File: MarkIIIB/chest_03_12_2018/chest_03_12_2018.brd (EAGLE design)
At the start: 24.9 x 22.3 mm, 15 parts, among them P100 503148-0890, U101 BNO055

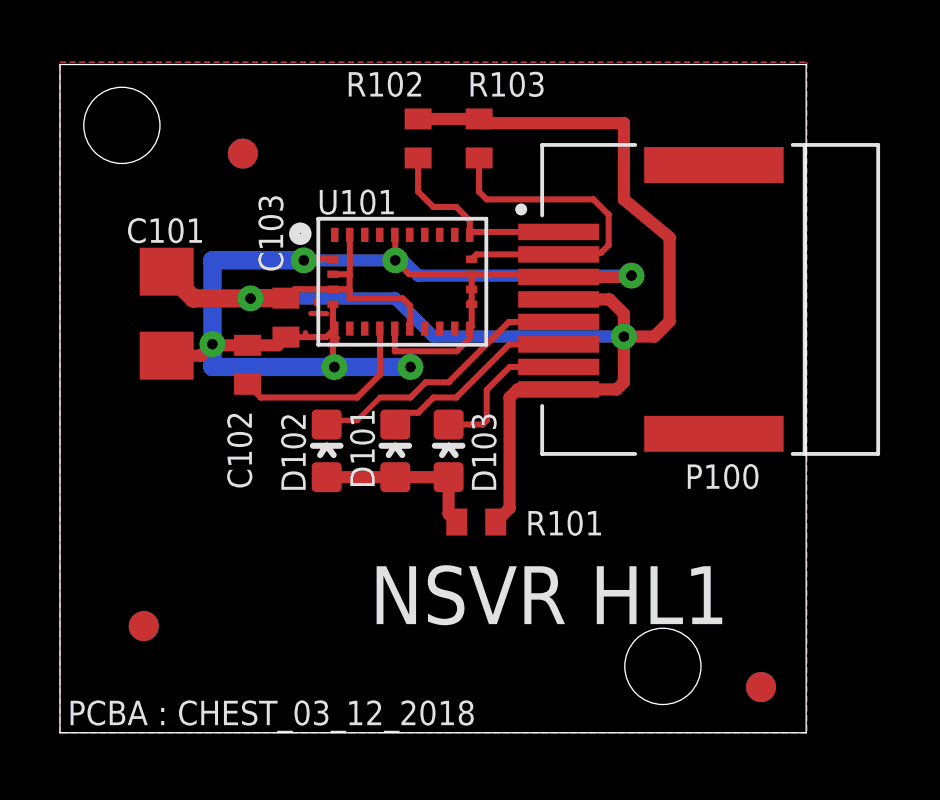
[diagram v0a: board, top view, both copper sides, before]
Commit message: Add Part Number ROllup Spreadsheets
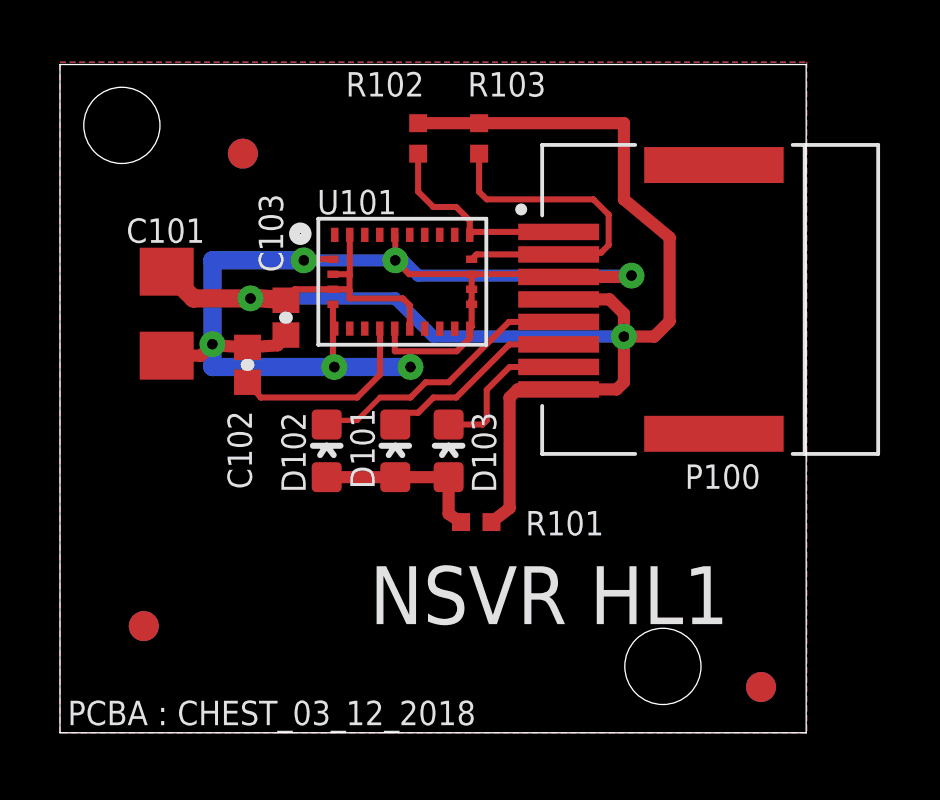
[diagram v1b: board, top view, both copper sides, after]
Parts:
- C102, C103: device rcl:C0402 -> PatternAgents-ProtoPads:0402-CAP
- R101, R102, R103: device rcl:R0402 -> PatternAgents-ProtoPads:EIA-0402
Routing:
- net GND: track 50.3 -> 47.5 mm
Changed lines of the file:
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@@
 <layer number="220" name="220bmp" color="21" fill="1" visible="no" active="no"/>
 <layer number="221" name="221bmp" color="22" fill="1" visible="no" active="no"/>
+<layer number="222" name="222bmp" color="23" fill="1" visible="no" active="no"/>
 <layer number="223" name="223bmp" color="24" fill="1" visible="no" active="no"/>
 <layer number="224" name="224bmp" color="25" fill="1" visible="no" active="no"/>
@@
 </autorouter>
 <elements>
-<element name="C103" library="rcl" package="C0402" value="0.1u" x="7.531103125" y="13.837159375" smashed="yes" rot="R270">
+<element name="C103" library="PatternAgents-ProtoPads" package="0402-CAP" value="0.1u" x="7.531103125" y="13.837159375" smashed="yes" rot="R270">
 <attribute name="NAME" x="6.6261" y="17.96440625" size="0.8128" layer="25" font="vector" ratio="15" rot="R270"/>
 </element>
-<element name="C102" library="rcl" package="C0402" value="0.1u" x="6.2519625" y="12.2656625" smashed="yes" rot="R90">
+<element name="C102" library="PatternAgents-ProtoPads" package="0402-CAP" value="0.1u" x="6.2519625" y="12.2656625" smashed="yes" rot="R90">
 <attribute name="NAME" x="6.398003125" y="8.1193625" size="0.8128" layer="25" font="vector" ratio="15" rot="R90"/>
 </element>
@@
 <attribute name="NAME" x="23.34826875" y="8.945234375" size="0.8128" layer="25" font="vector" ratio="15" rot="R180"/>
 </element>
-<element name="R101" library="rcl" package="R0402" value="220 Ohm" x="13.87500625" y="7.0238625" smashed="yes">
+<element name="R101" library="PatternAgents-ProtoPads" package="EIA-0402" value="220 Ohm" x="13.87500625" y="7.0238625" smashed="yes">
 <attribute name="NAME" x="15.517115625" y="6.579875" size="0.8128" layer="25" font="vector" ratio="15"/>
 </element>
@@
 </element>
 <element name="U$2" library="nsvr" package="NSVR_LOGO" value="" x="24.384" y="5.842" rot="MR0"/>
-<element name="R102" library="rcl" package="R0402" value="4K7" x="11.938" y="19.812" smashed="yes" rot="R90">
+<element name="R102" library="PatternAgents-ProtoPads" package="EIA-0402" value="4K7" x="11.938" y="19.812" smashed="yes" rot="R90">
 <attribute name="NAME" x="9.525" y="21.209" size="0.8128" layer="25" font="vector" ratio="20"/>
 <attribute name="VALUE" x="11.303" y="18.923" size="0.8128" layer="27" font="vector" ratio="20" rot="R90"/>
 </element>
-<element name="R103" library="rcl" package="R0402" value="4K7" x="13.97" y="19.812" smashed="yes" rot="R90">
+<element name="R103" library="PatternAgents-ProtoPads" package="EIA-0402" value="4K7" x="13.97" y="19.812" smashed="yes" rot="R90">
 <attribute name="NAME" x="13.589" y="21.209" size="0.8128" layer="25" font="vector" ratio="20"/>
 <attribute name="VALUE" x="13.335" y="18.923" size="0.8128" layer="27" font="vector" ratio="20" rot="R90"/>
@@
 <wire x1="9.0976875" y1="12.2383125" x2="9.144" y2="12.192" width="0.2032" layer="1"/>
 <via x="9.144" y="12.192" extent="1-16" drill="0.3556"/>
-<wire x1="7.531103125" y1="13.187159375" x2="8.875075" y2="13.187159375" width="0.2032" layer="1"/>
-<wire x1="8.875075" y1="13.187159375" x2="9.1601875" y2="13.472271875" width="0.2032" layer="1"/>
-<wire x1="6.2519625" y1="12.9156625" x2="7.25960625" y2="12.9156625" width="0.4064" layer="1"/>
-<wire x1="7.25960625" y1="12.9156625" x2="7.531103125" y2="13.187159375" width="0.4064" layer="1"/>
-<wire x1="5.1183375" y1="12.9156625" x2="6.2519625" y2="12.9156625" width="0.4064" layer="1"/>
+<wire x1="6.2519625" y1="12.8456625" x2="7.25960625" y2="12.9156625" width="0.4064" layer="1"/>
+<wire x1="7.25960625" y1="12.9156625" x2="7.531103125" y2="13.257159375" width="0.4064" layer="1"/>
+<wire x1="5.1183375" y1="12.9156625" x2="6.2519625" y2="12.8456625" width="0.4064" layer="1"/>
 <wire x1="3.556" y1="12.57" x2="4.696" y2="12.57" width="0.4064" layer="1"/>
 <wire x1="4.696" y1="12.57" x2="5.08" y2="12.954" width="0.4064" layer="1"/>
-<wire x1="6.2519625" y1="12.9156625" x2="6.3116625" y2="12.9156625" width="0.4064" layer="1"/>
+<wire x1="6.2519625" y1="12.8456625" x2="6.3116625" y2="12.9156625" width="0.4064" layer="1"/>
 <wire x1="6.3116625" y1="12.9156625" x2="6.35" y2="12.954" width="0.4064" layer="1"/>
 <wire x1="16.62226875" y1="15.195234375" x2="19.005234375" y2="15.195234375" width="0.4064" layer="1"/>
@@
 <wire x1="11.43" y1="15.748" x2="11.938" y2="15.24" width="0.4064" layer="16"/>
 <wire x1="11.938" y1="15.24" x2="19.05" y2="15.24" width="0.4064" layer="16"/>
-<wire x1="8.89" y1="13.97" x2="8.3621" y2="13.979340625" width="0.1778" layer="1"/>
-<wire x1="8.1788" y1="13.335" x2="8.1788" y2="13.235159375" width="0.1778" layer="1"/>
-<wire x1="8.5344" y1="14.4018" x2="8.5344" y2="14.302171875" width="0.1778" layer="1"/>
-<wire x1="9.2456" y1="13.1572" x2="9.16016875" y2="13.070975" width="0.1778" layer="1"/>
-<wire x1="9.0678" y1="12.9794" x2="8.99505625" y2="12.929971875" width="0.1778" layer="1"/>
-<wire x1="9.2456" y1="12.9794" x2="9.16016875" y2="12.929971875" width="0.1778" layer="1"/>
+<wire x1="13.6906" y1="14.224" x2="13.7226875" y2="14.284771875" width="0.1778" layer="1"/>
+<wire x1="13.7226875" y1="14.284771875" x2="13.7227" y2="14.284803125" width="0.1778" layer="1"/>
 <wire x1="13.6906" y1="14.4018" x2="13.7226875" y2="14.284771875" width="0.1778" layer="1"/>
 <wire x1="13.6906" y1="14.4018" x2="13.7227" y2="14.354971875" width="0.1778" layer="1"/>
-<wire x1="13.6906" y1="14.224" x2="13.7226875" y2="14.284771875" width="0.1778" layer="1"/>
-<wire x1="13.6906" y1="14.224" x2="13.7227" y2="14.284803125" width="0.1778" layer="1"/>
+<wire x1="13.335" y1="15.2908" x2="13.335" y2="15.284784375" width="0.1778" layer="1"/>
 </signal>
 <signal name="3.6V">
@@
 <via x="18.796" y="13.208" extent="1-16" drill="0.3556"/>
 <via x="6.35" y="14.478" extent="1-16" drill="0.3556"/>
-<wire x1="7.531103125" y1="14.487159375" x2="6.613159375" y2="14.487159375" width="0.6096" layer="1"/>
+<wire x1="7.531103125" y1="14.417159375" x2="6.613159375" y2="14.487159375" width="0.6096" layer="1"/>
 <wire x1="6.613159375" y1="14.487159375" x2="6.35" y2="14.478" width="0.4064" layer="1"/>
 <wire x1="9.0976875" y1="14.784771875" x2="7.828715625" y2="14.784771875" width="0.2032" layer="1"/>
-<wire x1="7.828715625" y1="14.784771875" x2="7.531103125" y2="14.487159375" width="0.2032" layer="1"/>
+<wire x1="7.828715625" y1="14.784771875" x2="7.531103125" y2="14.417159375" width="0.2032" layer="1"/>
 <wire x1="9.6601875" y1="16.597271875" x2="9.6601875" y2="15.2481875" width="0.2032" layer="1"/>
 <wire x1="9.6601875" y1="15.2481875" x2="9.652" y2="15.24" width="0.2032" layer="1"/>
@@
 <wire x1="15.255234375" y1="11.445234375" x2="14.986" y2="11.176" width="0.4064" layer="1"/>
 <wire x1="14.986" y1="11.176" x2="14.986" y2="7.48485625" width="0.4064" layer="1"/>
-<wire x1="14.986" y1="7.48485625" x2="14.52500625" y2="7.0238625" width="0.4064" layer="1"/>
+<wire x1="14.986" y1="7.48485625" x2="14.38300625" y2="7.0238625" width="0.4064" layer="1"/>
 <wire x1="11.43" y1="14.478" x2="9.652" y2="14.478" width="0.2032" layer="1"/>
 <wire x1="9.652" y1="14.478" x2="9.652" y2="14.732" width="0.2032" layer="1"/>
@@
 <wire x1="20.32" y1="13.716" x2="19.812" y2="13.208" width="0.4064" layer="1"/>
 <wire x1="19.812" y1="13.208" x2="18.796" y2="13.208" width="0.4064" layer="1"/>
-<wire x1="18.796" y1="20.32" x2="14.112" y2="20.32" width="0.4064" layer="1"/>
-<wire x1="14.112" y1="20.32" x2="13.97" y2="20.462" width="0.4064" layer="1"/>
-<wire x1="13.97" y1="20.462" x2="11.938" y2="20.462" width="0.4064" layer="1"/>
+<wire x1="18.796" y1="20.32" x2="13.97" y2="20.32" width="0.4064" layer="1"/>
+<wire x1="13.97" y1="20.32" x2="11.938" y2="20.32" width="0.4064" layer="1"/>
 </signal>
 <signal name="PWM_R">
@@
 <wire x1="10.668" y1="13.464459375" x2="10.6601875" y2="13.472271875" width="0.2032" layer="1"/>
 <wire x1="9.906" y1="11.176" x2="6.691625" y2="11.176" width="0.2032" layer="1"/>
-<wire x1="6.691625" y1="11.176" x2="6.2519625" y2="11.6156625" width="0.2032" layer="1"/>
+<wire x1="6.691625" y1="11.176" x2="6.2519625" y2="11.6856625" width="0.2032" layer="1"/>
 <wire x1="9.906" y1="11.176" x2="10.668" y2="11.938" width="0.2032" layer="1"/>
 </signal>
@@
 <wire x1="16.62226875" y1="16.695234375" x2="13.75815" y2="16.695234375" width="0.2032" layer="1"/>
 <wire x1="13.75815" y1="16.695234375" x2="13.6601875" y2="16.597271875" width="0.2032" layer="1"/>
-<wire x1="11.938" y1="19.162" x2="11.938" y2="18.034" width="0.2032" layer="1"/>
+<wire x1="11.938" y1="19.304" x2="11.938" y2="18.034" width="0.2032" layer="1"/>
 <wire x1="11.938" y1="18.034" x2="12.446" y2="17.526" width="0.2032" layer="1"/>
 <wire x1="12.446" y1="17.526" x2="13.208" y2="17.526" width="0.2032" layer="1"/>
@@
 <wire x1="16.62226875" y1="15.945234375" x2="13.88315" y2="15.945234375" width="0.2032" layer="1"/>
 <wire x1="13.88315" y1="15.945234375" x2="13.7226875" y2="15.784771875" width="0.2032" layer="1"/>
-<wire x1="13.97" y1="19.162" x2="13.97" y2="18.034" width="0.2032" layer="1"/>
+<wire x1="13.97" y1="19.304" x2="13.97" y2="18.034" width="0.2032" layer="1"/>
 <wire x1="13.97" y1="18.034" x2="14.224" y2="17.78" width="0.2032" layer="1"/>
 <wire x1="14.224" y1="17.78" x2="17.78" y2="17.78" width="0.2032" layer="1"/>
@@
 <wire x1="11.176" y1="8.521" x2="12.954" y2="8.521" width="0.4064" layer="1"/>
 <wire x1="12.954" y1="8.521" x2="12.954" y2="7.29486875" width="0.4064" layer="1"/>
-<wire x1="12.954" y1="7.29486875" x2="13.22500625" y2="7.0238625" width="0.4064" layer="1"/>
+<wire x1="12.954" y1="7.29486875" x2="13.36700625" y2="7.0238625" width="0.4064" layer="1"/>
 </signal>
 </signals>
